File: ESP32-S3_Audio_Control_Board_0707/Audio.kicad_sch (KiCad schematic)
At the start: 22 parts, among them U4 TAS5805MPWPR

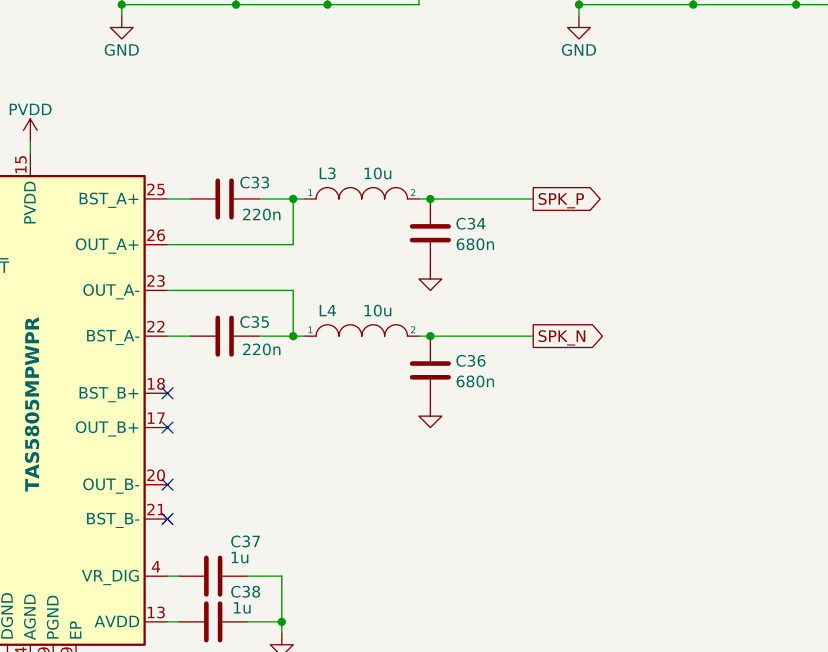
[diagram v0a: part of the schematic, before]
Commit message: update TAS5805, 4-layer
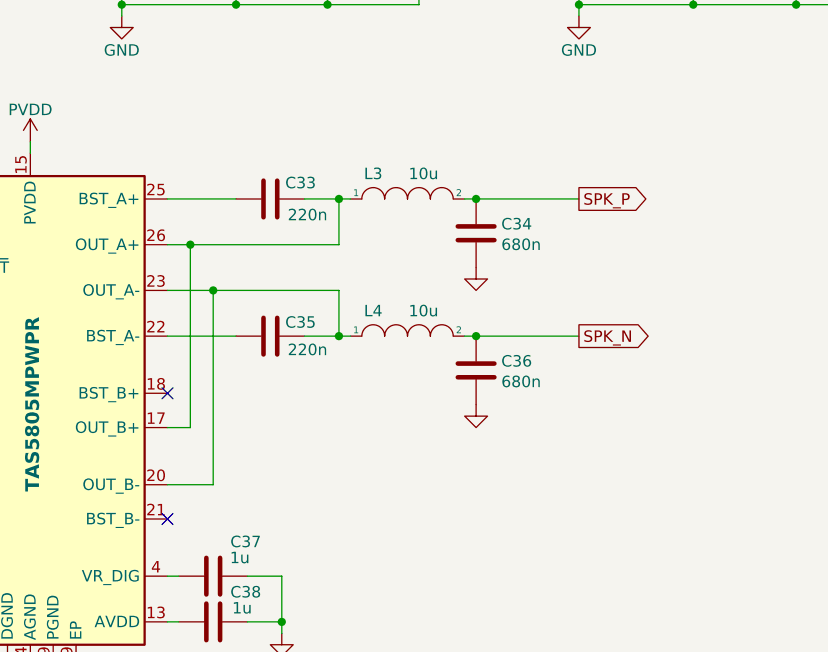
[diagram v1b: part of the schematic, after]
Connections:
- net at C35.2, L4.1, U4.23 (OUT_A-): now also U4.20 (OUT_B-)
- net at U4.17 (OUT_B+): now also C33.2, L3.1, U4.26 (OUT_A+)
- no-connect marks 5 -> 3
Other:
- moved on the sheet: C33, C34, C35, C36, L3, L4
